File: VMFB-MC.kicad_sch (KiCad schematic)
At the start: 51 parts, among them J1 DISPENSE, J10 PIR, J2 EMPTY, J3 DISPENSE, J4 DEPOSIT, J5 Conn_01x03_Pin, J6 DISPENSE, J7 EMPTY, J8 MOTOR, J9 Conn_01x10_Pin, Q1 Q_Photo_NPN, Q10 Q_Photo_NPN, Q2 Q_Photo_NPN, Q3 Q_Photo_NPN, Q4 Q_Photo_NPN, Q5 Q_Photo_NPN, Q6 Q_Photo_NPN, Q7 TIP120, Q8 TIP120, Q9 BC337, U1 LM393

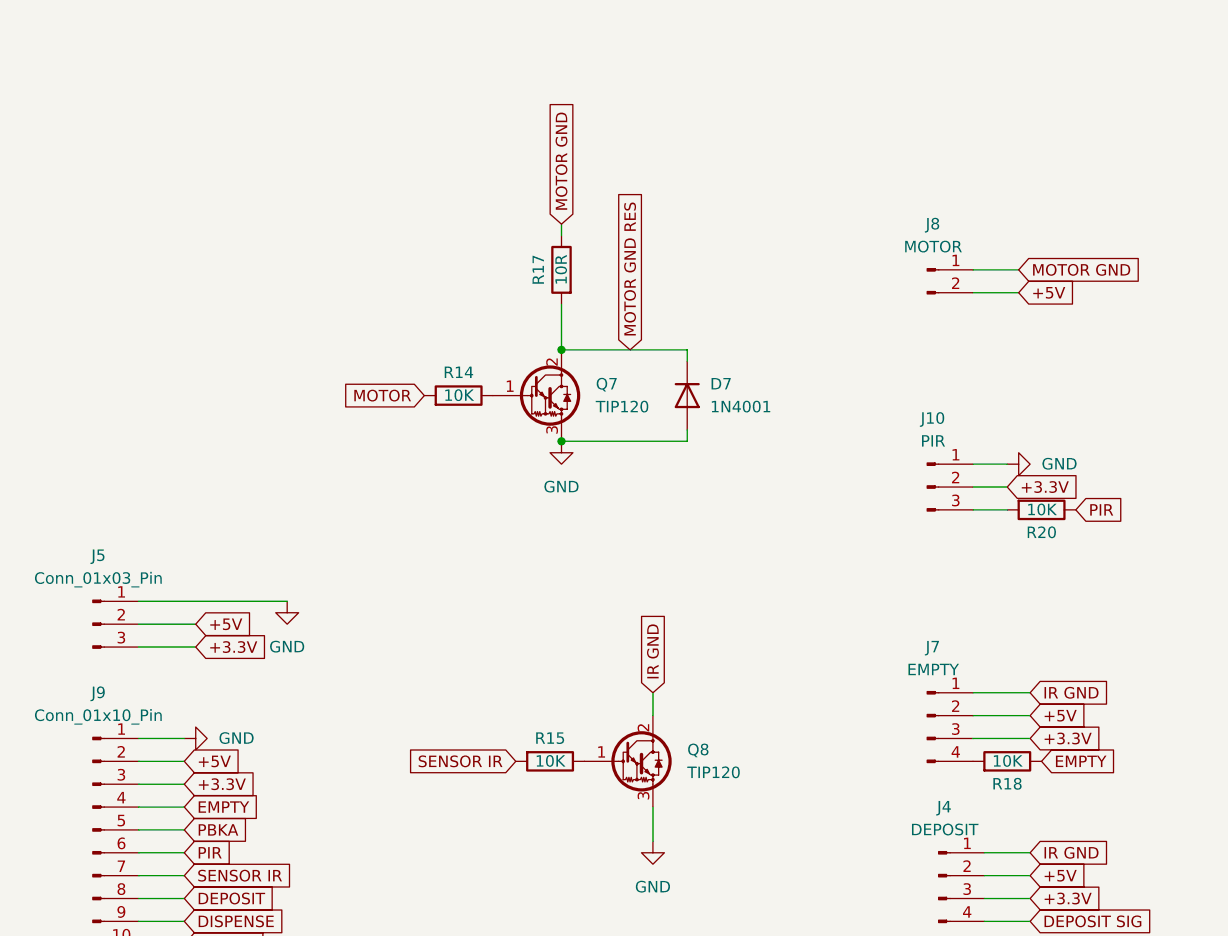
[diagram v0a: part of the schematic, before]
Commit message: removed 10R motor resistor and extra power header, revised placement
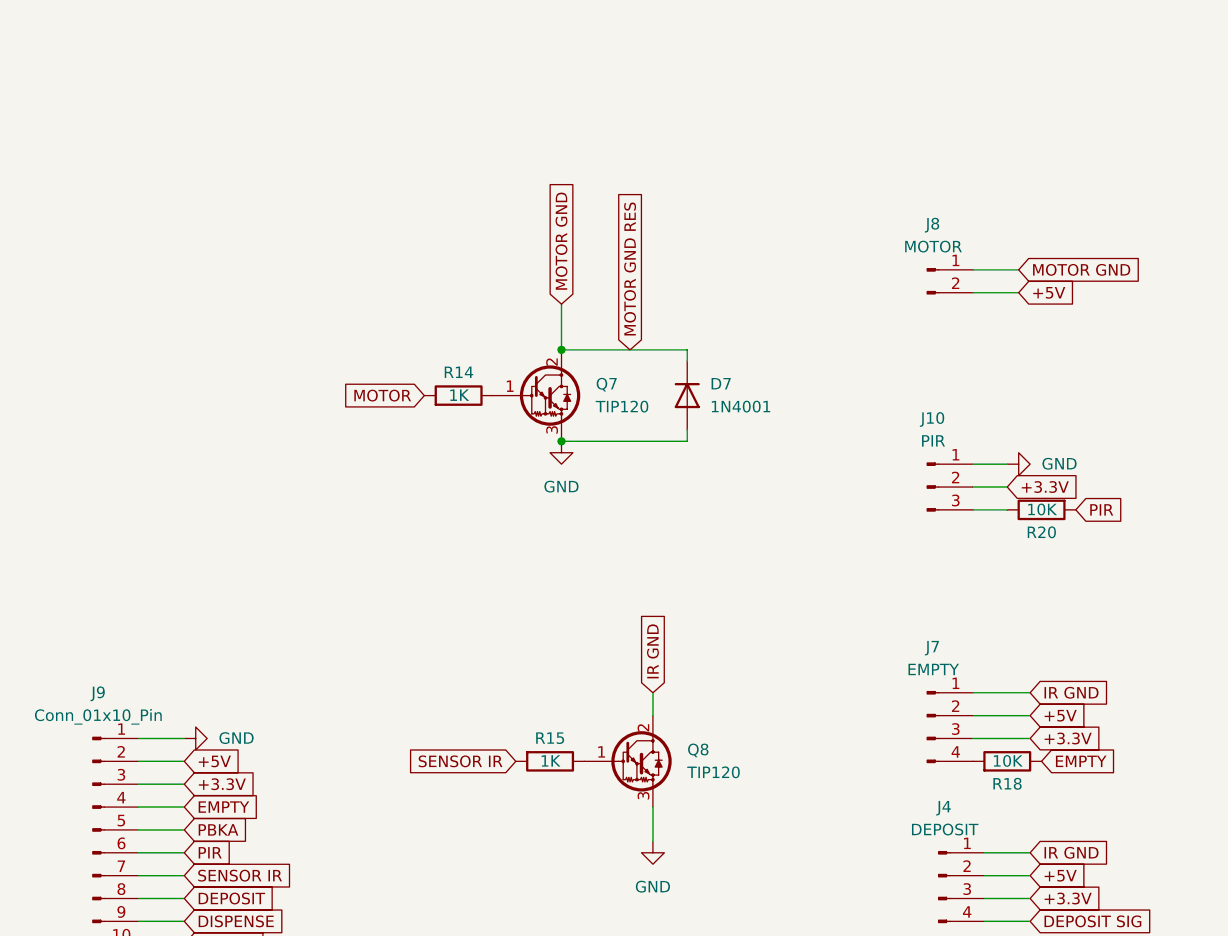
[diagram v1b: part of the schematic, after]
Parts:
- removed J5: Conn_01x03_Pin, Connector_PinHeader_2.54mm:PinHeader_1x03_P2.54mm_Vertical, symbol Connector:Conn_01x03_Pin
- removed R17: 10R, Resistor_THT:R_Axial_DIN0414_L11.9mm_D4.5mm_P5.08mm_Vertical, symbol Device:R
- R14, R15: value 10K -> 1K
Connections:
- net MOTOR GND RES is gone; now on net MOTOR GND: D7.1 (K), Q7.2 (C)
- net PIR: now also R20.2; no longer R20.1
- net at J10.3 (Pin_3): now also R20.1; no longer R20.2
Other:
- moved on the sheet: R20
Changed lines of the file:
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@@
-    (stroke (width 0) (type default))
-  )
-  (wire (pts (xy 90.17 41.91) (xy 90.17 43.18))
     (stroke (width 0) (type default))
   )
@@
     (stroke (width 0) (type default))
   )
-  (wire (pts (xy 49.53 86.36) (xy 43.18 86.36))
-    (stroke (width 0) (type default))
-  )
   (wire (pts (xy 217.17 123.19) (xy 231.14 123.19))
     (stroke (width 0) (type default))
@@
     (stroke (width 0) (type default))
   )
-  (wire (pts (xy 49.53 88.9) (xy 43.18 88.9))
-    (stroke (width 0) (type default))
-  )
   (wire (pts (xy 100.33 110.49) (xy 100.33 106.68))
     (stroke (width 0) (type default))
@@
     (stroke (width 0) (type default))
   )
-  (wire (pts (xy 90.17 55.88) (xy 90.17 50.8))
+  (wire (pts (xy 90.17 50.8) (xy 90.17 55.88))
     (stroke (width 0) (type default))
   )
@@
     (stroke (width 0) (type default))
   )
-  (wire (pts (xy 43.18 83.82) (xy 59.69 83.82))
-    (stroke (width 0) (type default))
-  )
   (wire (pts (xy 104.14 66.04) (xy 104.14 64.77))
     (stroke (width 0) (type default))
@@
   (wire (pts (xy 231.14 138.43) (xy 245.11 138.43))
     (stroke (width 0) (type default))
-  )
-  (global_label "+3.3V" (shape input) (at 49.53 88.9 0) (fields_autoplaced)
-    (effects (font (size 1.27 1.27)) (justify left))
-    (property "Intersheetrefs" "${INTERSHEET_REFS}" (at 58.2 88.9 0)
-      (effects (font (size 1.27 1.27)) (justify left) hide)
-    )
   )
   (global_label "DISPENSE SIG" (shape input) (at 144.78 137.16 0) (fields_autoplaced)
@@
     )
   )
-  (global_label "MOTOR GND" (shape input) (at 90.17 41.91 90) (fields_autoplaced)
-    (effects (font (size 1.27 1.27)) (justify left))
-    (property "Intersheetrefs" "${INTERSHEET_REFS}" (at 90.17 27.7367 90)
+  (global_label "MOTOR GND" (shape input) (at 90.17 50.8 90) (fields_autoplaced)
+    (effects (font (size 1.27 1.27)) (justify left))
+    (property "Intersheetrefs" "${INTERSHEET_REFS}" (at 90.17 36.6267 90)
       (effects (font (size 1.27 1.27)) (justify left) hide)
     )
@@
     (effects (font (size 1.27 1.27)) (justify left))
     (property "Intersheetrefs" "${INTERSHEET_REFS}" (at 157.0785 119.38 0)
-      (effects (font (size 1.27 1.27)) (justify left) hide)
-    )
-  )
-  (global_label "+5V" (shape input) (at 49.53 86.36 0) (fields_autoplaced)
-    (effects (font (size 1.27 1.27)) (justify left))
-    (property "Intersheetrefs" "${INTERSHEET_REFS}" (at 56.3857 86.36 0)
       (effects (font (size 1.27 1.27)) (justify left) hide)
     )
@@
       (effects (font (size 1.27 1.27)))
     )
-    (property "Value" "10K" (at 88.9 101.6 90)
+    (property "Value" "1K" (at 88.9 101.6 90)
       (effects (font (size 1.27 1.27)))
     )
@@
     )
   )
-  (symbol (lib_id "power:GND") (at 59.69 83.82 0) (unit 1)
-    (in_bom yes) (on_board yes) (dnp no) (fields_autoplaced)
-    (property "Reference" "#PWR06" (at 59.69 90.17 0)
-      (effects (font (size 1.27 1.27)) hide)
-    )
-    (property "Value" "GND" (at 59.69 88.9 0)
-      (effects (font (size 1.27 1.27)))
-    )
-    (property "Footprint" "" (at 59.69 83.82 0)
-      (effects (font (size 1.27 1.27)) hide)
-    )
-    (property "Datasheet" "" (at 59.69 83.82 0)
-      (effects (font (size 1.27 1.27)) hide)
-    )
-    (pin "1")
-    (instances
-      (project "VMFB-MC"
-        (path "/21047f2f-d4ba-4d74-abfd-549d2dbb0ef3"
-          (reference "#PWR06") (unit 1)
-        )
-      )
-    )
-  )
   (symbol (lib_id "Connector:Conn_01x04_Pin") (at 130.81 96.52 0) (unit 1)
     (in_bom yes) (on_board yes) (dnp no) (fields_autoplaced)
@@
     )
   )
-  (symbol (lib_id "Device:R") (at 143.51 73.66 270) (unit 1)
+  (symbol (lib_id "Device:R") (at 143.51 73.66 90) (mirror x) (unit 1)
     (in_bom yes) (on_board yes) (dnp no)
     (property "Reference" "R20" (at 143.51 76.2 90)
@@
       (effects (font (size 1.27 1.27)))
     )
-    (property "Value" "10K" (at 78.74 60.96 90)
+    (property "Value" "1K" (at 78.74 60.96 90)
       (effects (font (size 1.27 1.27)))
     )
@@
     )
   )
-  (symbol (lib_id "Device:R") (at 90.17 46.99 0) (mirror y) (unit 1)
-    (in_bom yes) (on_board yes) (dnp no)
-    (property "Reference" "R17" (at 87.63 46.99 90)
-      (effects (font (size 1.27 1.27)))
-    )
-    (property "Value" "10R" (at 90.17 46.99 90)
-      (effects (font (size 1.27 1.27)))
-    )
-    (property "Footprint" "Resistor_THT:R_Axial_DIN0414_L11.9mm_D4.5mm_P5.08mm_Vertical" (at 91.948 46.99 90)
-      (effects (font (size 1.27 1.27)) hide)
-    )
-    (property "Datasheet" "~" (at 90.17 46.99 0)
-      (effects (font (size 1.27 1.27)) hide)
-    )
-    (pin "1")
-    (pin "2")
-    (instances
-      (project "VMFB-MC"
-        (path "/21047f2f-d4ba-4d74-abfd-549d2dbb0ef3"
-          (reference "R17") (unit 1)
-        )
-      )
-    )
-  )
   (symbol (lib_id "Connector:Conn_01x04_Pin") (at 224.79 95.25 0) (unit 1)
     (in_bom yes) (on_board yes) (dnp no) (fields_autoplaced)
@@
         )
       )
-    )
-  )
-  (symbol (lib_id "Connector:Conn_01x03_Pin") (at 38.1 86.36 0) (unit 1)
-    (in_bom yes) (on_board yes) (dnp no) (fields_autoplaced)
-    (property "Reference" "J5" (at 38.735 78.74 0)
-      (effects (font (size 1.27 1.27)))
-    )
-    (property "Value" "Conn_01x03_Pin" (at 38.735 81.28 0)
-      (effects (font (size 1.27 1.27)))
-    )
-    (property "Footprint" "Connector_PinHeader_2.54mm:PinHeader_1x03_P2.54mm_Vertical" (at 38.1 86.36 0)
-      (effects (font (size 1.27 1.27)) hide)
-    )
-    (property "Datasheet" "~" (at 38.1 86.36 0)
-      (effects (font (size 1.27 1.27)) hide)
-    )
-    (pin "1")
-    (pin "2")
-    (pin "3")
-    (instances
-      (project "VMFB-MC"
-        (path "/21047f2f-d4ba-4d74-abfd-549d2dbb0ef3"
-          (reference "J5") (unit 1)
-        )
-      )

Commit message: reannotated
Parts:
- renumbered J7 to J4, J4 to J5, J8 to J7, J10 to J8, R8 to R12, R9 to R13, R20 to R16, R18 to R17, R19 to R18, R16 to R19, R12 to R8, R13 to R9
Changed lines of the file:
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@@
   (symbol (lib_id "Device:R") (at 139.7 101.6 270) (mirror x) (unit 1)
     (in_bom yes) (on_board yes) (dnp no)
-    (property "Reference" "R18" (at 139.7 104.14 90)
+    (property "Reference" "R17" (at 139.7 104.14 90)
       (effects (font (size 1.27 1.27)))
     )
@@
       (project "VMFB-MC"
         (path "/21047f2f-d4ba-4d74-abfd-549d2dbb0ef3"
-          (reference "R18") (unit 1)
+          (reference "R17") (unit 1)
         )
       )
@@
   (symbol (lib_id "Device:R") (at 227.33 59.69 270) (mirror x) (unit 1)
     (in_bom yes) (on_board yes) (dnp no)
-    (property "Reference" "R9" (at 227.33 57.15 90)
+    (property "Reference" "R13" (at 227.33 57.15 90)
       (effects (font (size 1.27 1.27)))
     )
@@
       (project "VMFB-MC"
         (path "/21047f2f-d4ba-4d74-abfd-549d2dbb0ef3"
-          (reference "R9") (unit 1)
+          (reference "R13") (unit 1)
         )
       )
@@
   (symbol (lib_id "Device:R") (at 227.33 35.56 90) (unit 1)
     (in_bom yes) (on_board yes) (dnp no)
-    (property "Reference" "R8" (at 227.33 33.02 90)
+    (property "Reference" "R12" (at 227.33 33.02 90)
       (effects (font (size 1.27 1.27)))
     )
@@
       (project "VMFB-MC"
         (path "/21047f2f-d4ba-4d74-abfd-549d2dbb0ef3"
-          (reference "R8") (unit 1)
+          (reference "R12") (unit 1)
         )
       )
@@
   (symbol (lib_id "Device:R") (at 208.28 29.21 0) (mirror x) (unit 1)
     (in_bom yes) (on_board yes) (dnp no)
-    (property "Reference" "R12" (at 209.55 30.48 0)
+    (property "Reference" "R8" (at 209.55 30.48 0)
       (effects (font (size 1.27 1.27)) (justify left))
     )
@@
       (project "VMFB-MC"
         (path "/21047f2f-d4ba-4d74-abfd-549d2dbb0ef3"
-          (reference "R12") (unit 1)
+          (reference "R8") (unit 1)
         )
       )
@@
   (symbol (lib_id "Connector:Conn_01x04_Pin") (at 130.81 96.52 0) (unit 1)
     (in_bom yes) (on_board yes) (dnp no) (fields_autoplaced)
-    (property "Reference" "J7" (at 131.445 88.9 0)
+    (property "Reference" "J4" (at 131.445 88.9 0)
       (effects (font (size 1.27 1.27)))
     )
@@
       (project "VMFB-MC"
         (path "/21047f2f-d4ba-4d74-abfd-549d2dbb0ef3"
-          (reference "J7") (unit 1)
+          (reference "J4") (unit 1)
         )
       )
@@
   (symbol (lib_id "Device:R") (at 208.28 53.34 0) (mirror x) (unit 1)
     (in_bom yes) (on_board yes) (dnp no)
-    (property "Reference" "R13" (at 209.55 53.34 0)
+    (property "Reference" "R9" (at 209.55 53.34 0)
       (effects (font (size 1.27 1.27)) (justify left))
     )
@@
       (project "VMFB-MC"
         (path "/21047f2f-d4ba-4d74-abfd-549d2dbb0ef3"
-          (reference "R13") (unit 1)
+          (reference "R9") (unit 1)
         )
       )
@@
   (symbol (lib_id "Device:R") (at 143.51 73.66 90) (mirror x) (unit 1)
     (in_bom yes) (on_board yes) (dnp no)
-    (property "Reference" "R20" (at 143.51 76.2 90)
+    (property "Reference" "R16" (at 143.51 76.2 90)
       (effects (font (size 1.27 1.27)))
     )
@@
       (project "VMFB-MC"
         (path "/21047f2f-d4ba-4d74-abfd-549d2dbb0ef3"
-          (reference "R20") (unit 1)
+          (reference "R16") (unit 1)
         )
       )
@@
   (symbol (lib_id "Connector:Conn_01x04_Pin") (at 132.08 114.3 0) (unit 1)
     (in_bom yes) (on_board yes) (dnp no) (fields_autoplaced)
-    (property "Reference" "J4" (at 132.715 106.68 0)
+    (property "Reference" "J5" (at 132.715 106.68 0)
       (effects (font (size 1.27 1.27)))
     )
@@
       (project "VMFB-MC"
         (path "/21047f2f-d4ba-4d74-abfd-549d2dbb0ef3"
-          (reference "J4") (unit 1)
+          (reference "J5") (unit 1)
         )
       )
@@
   (symbol (lib_id "Connector:Conn_01x03_Pin") (at 130.81 71.12 0) (unit 1)
     (in_bom yes) (on_board yes) (dnp no) (fields_autoplaced)
-    (property "Reference" "J10" (at 131.445 63.5 0)
+    (property "Reference" "J8" (at 131.445 63.5 0)
       (effects (font (size 1.27 1.27)))
     )
@@
       (project "VMFB-MC"
         (path "/21047f2f-d4ba-4d74-abfd-549d2dbb0ef3"
-          (reference "J10") (unit 1)
+          (reference "J8") (unit 1)
         )
       )
@@
   (symbol (lib_id "Device:R") (at 100.33 140.97 0) (mirror x) (unit 1)
     (in_bom yes) (on_board yes) (dnp no)
-    (property "Reference" "R19" (at 101.6 140.97 0)
+    (property "Reference" "R18" (at 101.6 140.97 0)
       (effects (font (size 1.27 1.27)) (justify left))
     )
@@
       (project "VMFB-MC"
         (path "/21047f2f-d4ba-4d74-abfd-549d2dbb0ef3"
-          (reference "R19") (unit 1)
+          (reference "R18") (unit 1)
         )
       )
@@
   (symbol (lib_id "Device:R") (at 88.9 149.86 270) (unit 1)
     (in_bom yes) (on_board yes) (dnp no)
-    (property "Reference" "R16" (at 88.9 147.32 90)
+    (property "Reference" "R19" (at 88.9 147.32 90)
       (effects (font (size 1.27 1.27)))
     )
@@
       (project "VMFB-MC"
         (path "/21047f2f-d4ba-4d74-abfd-549d2dbb0ef3"
-          (reference "R16") (unit 1)
+          (reference "R19") (unit 1)
         )
       )
@@
   (symbol (lib_id "Connector:Conn_01x02_Pin") (at 130.81 46.99 0) (unit 1)
     (in_bom yes) (on_board yes) (dnp no) (fields_autoplaced)
-    (property "Reference" "J8" (at 131.445 41.91 0)
+    (property "Reference" "J7" (at 131.445 41.91 0)
       (effects (font (size 1.27 1.27)))
     )
@@
       (project "VMFB-MC"
         (path "/21047f2f-d4ba-4d74-abfd-549d2dbb0ef3"
-          (reference "J8") (unit 1)
-        )
-      )
+          (reference "J7") (unit 1)
+        )
+      )

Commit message: reduced footprint
footprint is now 65x68mm
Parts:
- removed J9: Conn_01x10_Pin, Connector_PinHeader_2.54mm:PinHeader_1x10_P2.54mm_Vertical, symbol Connector:Conn_01x10_Pin
- removed Q9: BC337, Package_TO_SOT_THT:TO-92_Inline_Wide, symbol Transistor_BJT:BC337
- removed R18: 47R, Resistor_THT:R_Axial_DIN0309_L9.0mm_D3.2mm_P2.54mm_Vertical, symbol Device:R
- removed R19: 10K, Resistor_THT:R_Axial_DIN0207_L6.3mm_D2.5mm_P2.54mm_Vertical, symbol Device:R
- added J10: Conn_01x05_Pin, Connector_PinHeader_2.54mm:PinHeader_1x05_P2.54mm_Vertical, symbol Connector:Conn_01x05_Pin
- added J6: Conn_01x04_Pin, Connector_PinHeader_2.54mm:PinHeader_1x04_P2.54mm_Vertical, symbol Connector:Conn_01x04_Pin
- renumbered J7 to J4, J8 to J5, J4 to J7, J5 to J8, J6 to J9, Q10 to Q9
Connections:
- net +3.3V: now also J10.3 (Pin_3)
- net +5V: now also J10.2 (Pin_2)
- net DEPOSIT: now also J6.1 (Pin_1)
- net DISPENSE: now also J6.2 (Pin_2)
- net DISPENSE SIG: now also R11.1; no longer R11.2
- net EMPTY: now also J10.5 (Pin_5)
- net GND: now also R8.1, J10.1 (Pin_1); no longer R8.2
- net MOTOR: now also J10.4 (Pin_4)
- net PIR: now also J6.4 (Pin_4)
- net SENSOR IR: now also J6.3 (Pin_3)
- net at R9.1, U1.3 (+): now also R11.2; no longer R11.1
- net at R10.1, U1.5 (+): now also R8.2; no longer R8.1
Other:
- moved on the sheet: R11
